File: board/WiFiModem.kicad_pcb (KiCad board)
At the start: 2 copper layers, 88.9 x 57.2 mm, 34 parts, among them J1 DB9_Female, J2 DB25_Male, J3 Barrel_Jack_Switch, J4 PRG, SW1 SW_Push, SW2 SW_Push, U1 ESP-12E, U2 LM7805_TO220, U3 MAX232, U4 LT1117-3.3

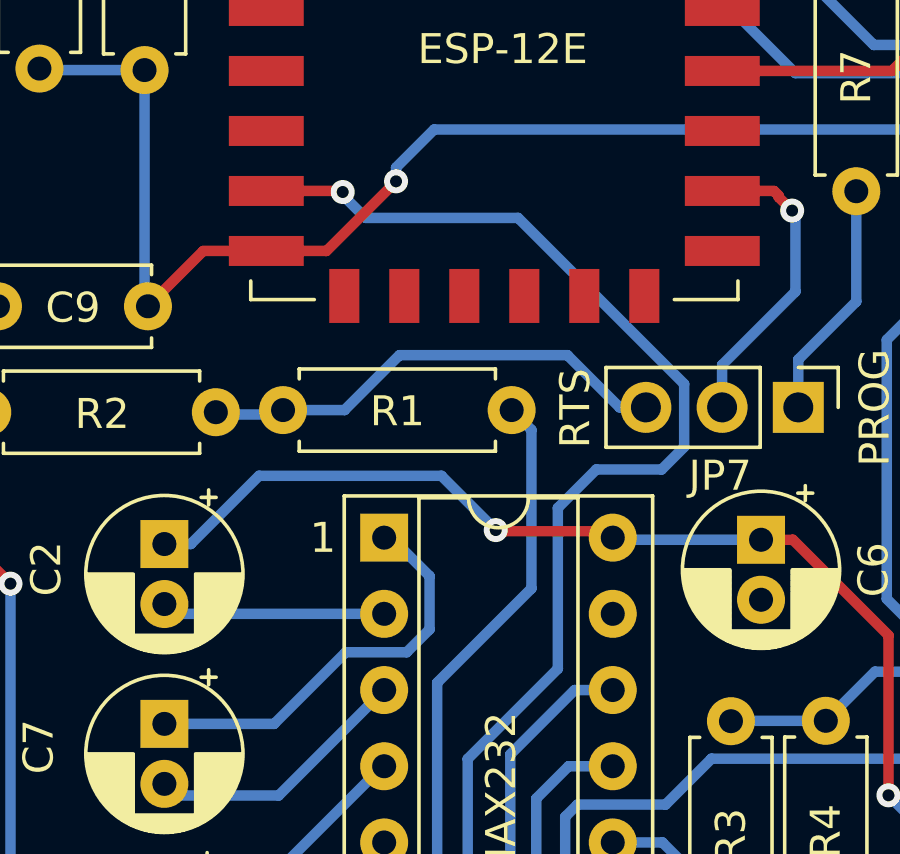
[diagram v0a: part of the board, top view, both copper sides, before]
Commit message: swap RTS and CTS
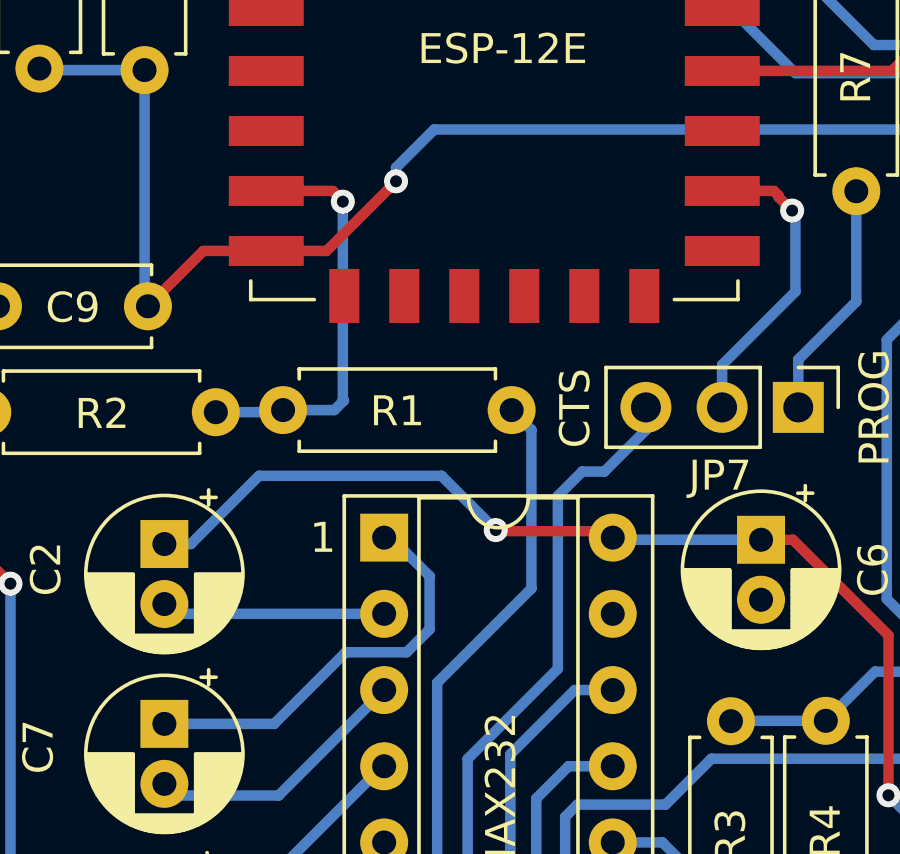
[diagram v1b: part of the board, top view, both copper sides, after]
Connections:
- JP7 pad 3: Net-(R1-Pad2) -> Net-(JP7-Pad3)
- U1 pad 7: Net-(U1-Pad7) -> Net-(R1-Pad2)
- U3 pad 10: Net-(U1-Pad7) -> Net-(JP7-Pad3)
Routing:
- net Net-(U1-Pad7): track 45.8 -> 0.00 mm, vias 2 -> 0
- net Net-(JP7-Pad3): track 0.00 -> 27.0 mm, vias 0 -> 1
- net Net-(R1-Pad2): track 15.9 -> 13.7 mm, vias 0 -> 1

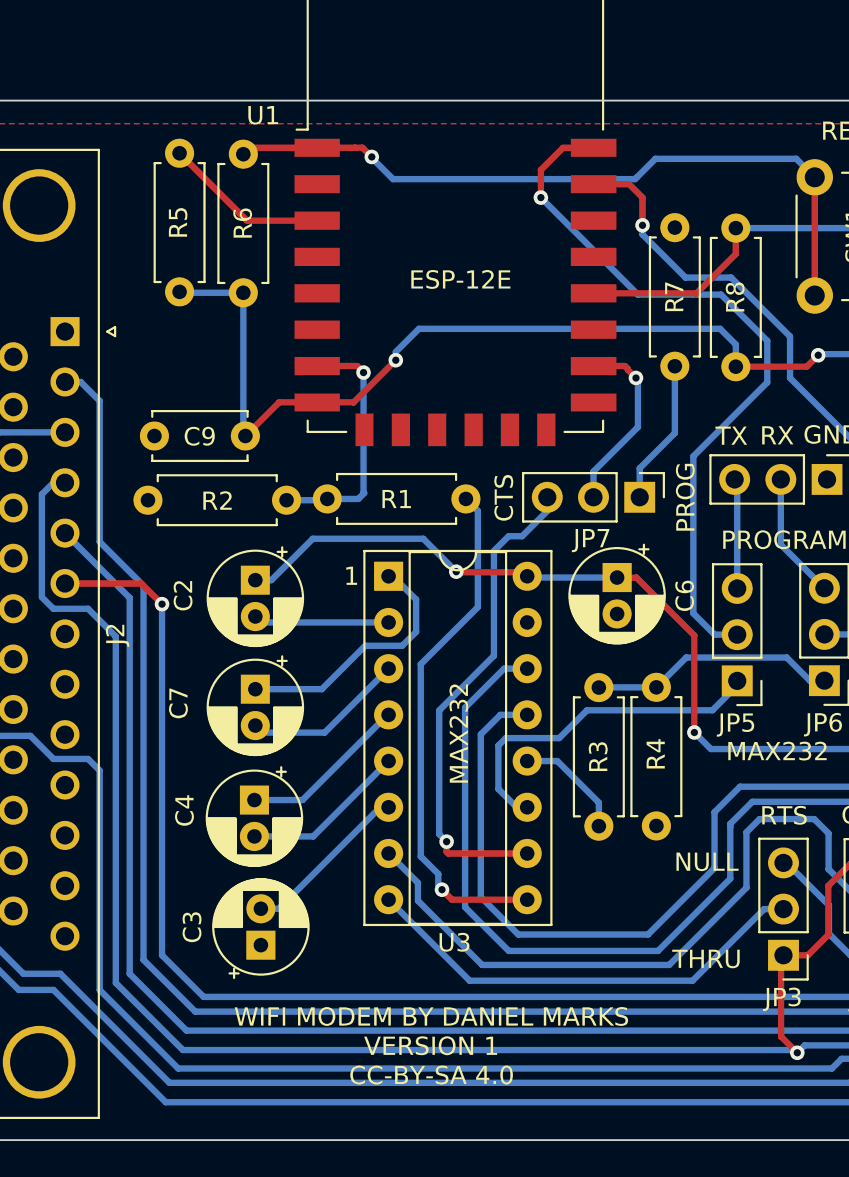
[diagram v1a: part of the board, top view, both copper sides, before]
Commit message: Added flow control enable GPIO
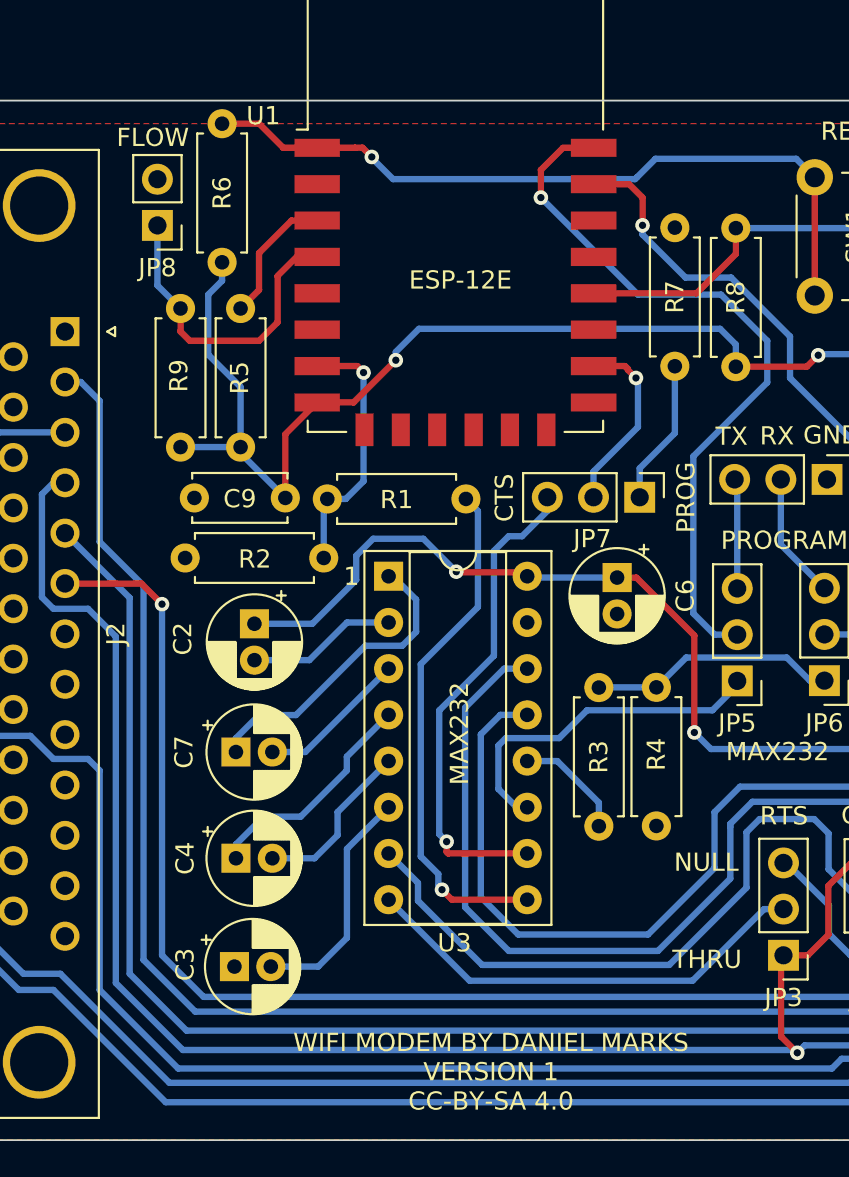
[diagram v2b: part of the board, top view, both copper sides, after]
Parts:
- added JP8: RTSCTS, Connector_PinHeader_2.54mm:PinHeader_1x02_P2.54mm_Vertical, F.Cu at (87.6, 76.7)
- added R9: 10k, Resistor_THT:R_Axial_DIN0207_L6.3mm_D2.5mm_P7.62mm_Horizontal, F.Cu at (88.9, 81.3)
- moved R5 9.17 mm to (92.2, 88.9)
- moved C9 4.05 mm to (89.7, 91.7)
- moved R2 3.78 mm to (96.8, 95.0)
- moved C7 3.62 mm to (91.9, 105.7), turned to 0 degrees
- moved C4 3.36 mm to (91.9, 111.5), turned to 0 degrees
- moved C2 2.40 mm to (93.0, 98.6)
- moved R6 2.04 mm to (91.2, 78.7)
- moved C3 1.87 mm to (91.9, 117.5), turned to 0 degrees
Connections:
- U1 pad 4: unconnected-(U1-Pad4) -> Net-(U1-Pad4)
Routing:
- net Net-(U1-Pad4): track 0.00 -> 17.5 mm
- net +3V3: track 81.1 -> 89.2 mm
- net Net-(C3-Pad2): track 9.33 -> 13.0 mm
- net Net-(C4-Pad1): track 9.32 -> 12.6 mm
- net Net-(C7-Pad1): track 14.0 -> 16.9 mm
- net +5V: track 105.6 -> 107.4 mm
- net Net-(R5-Pad2): track 9.10 -> 7.40 mm
- net Net-(R6-Pad2): track 39.7 -> 41.3 mm
- net Net-(R1-Pad2): track 13.7 -> 14.5 mm
- net Net-(C2-Pad2): track 7.46 -> 8.23 mm
- net Net-(C7-Pad2): track 8.94 -> 8.29 mm
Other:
- board text added: "FLOW"

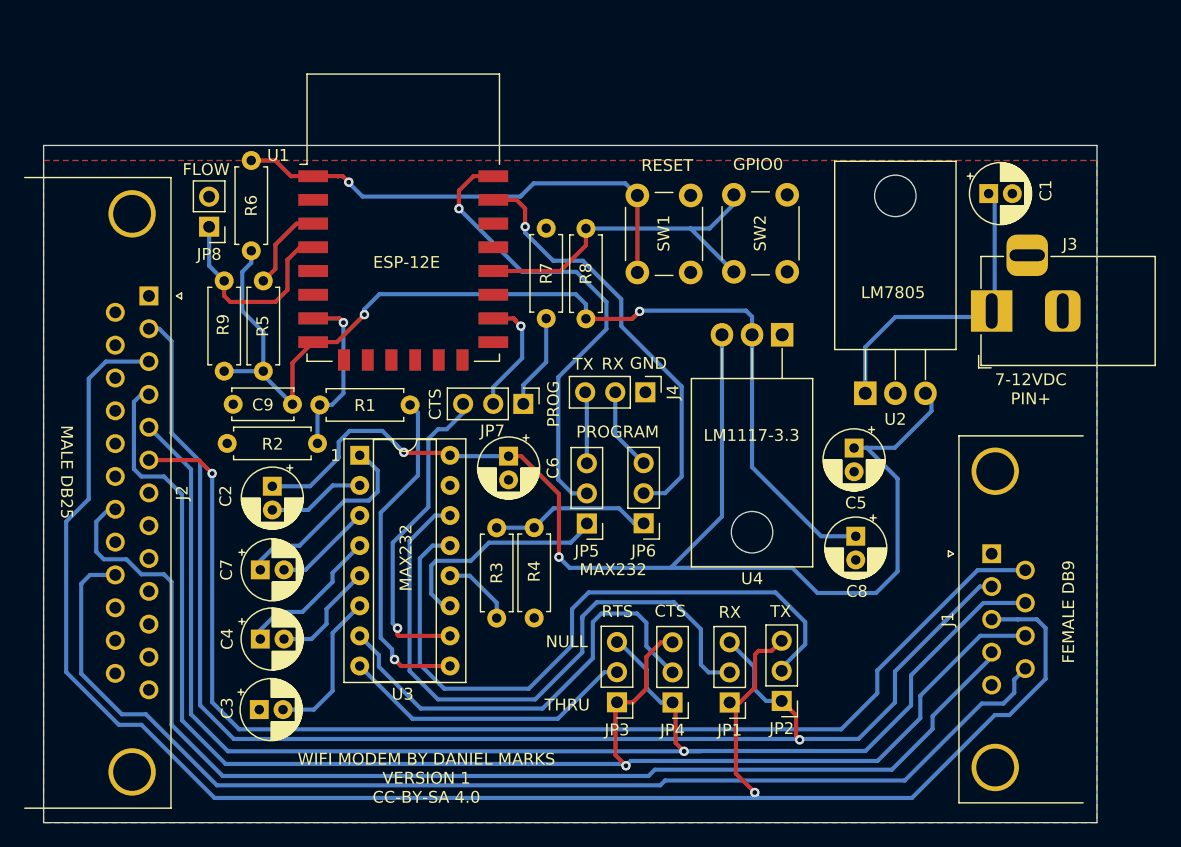
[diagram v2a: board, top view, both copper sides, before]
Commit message: Added all of the other control signals
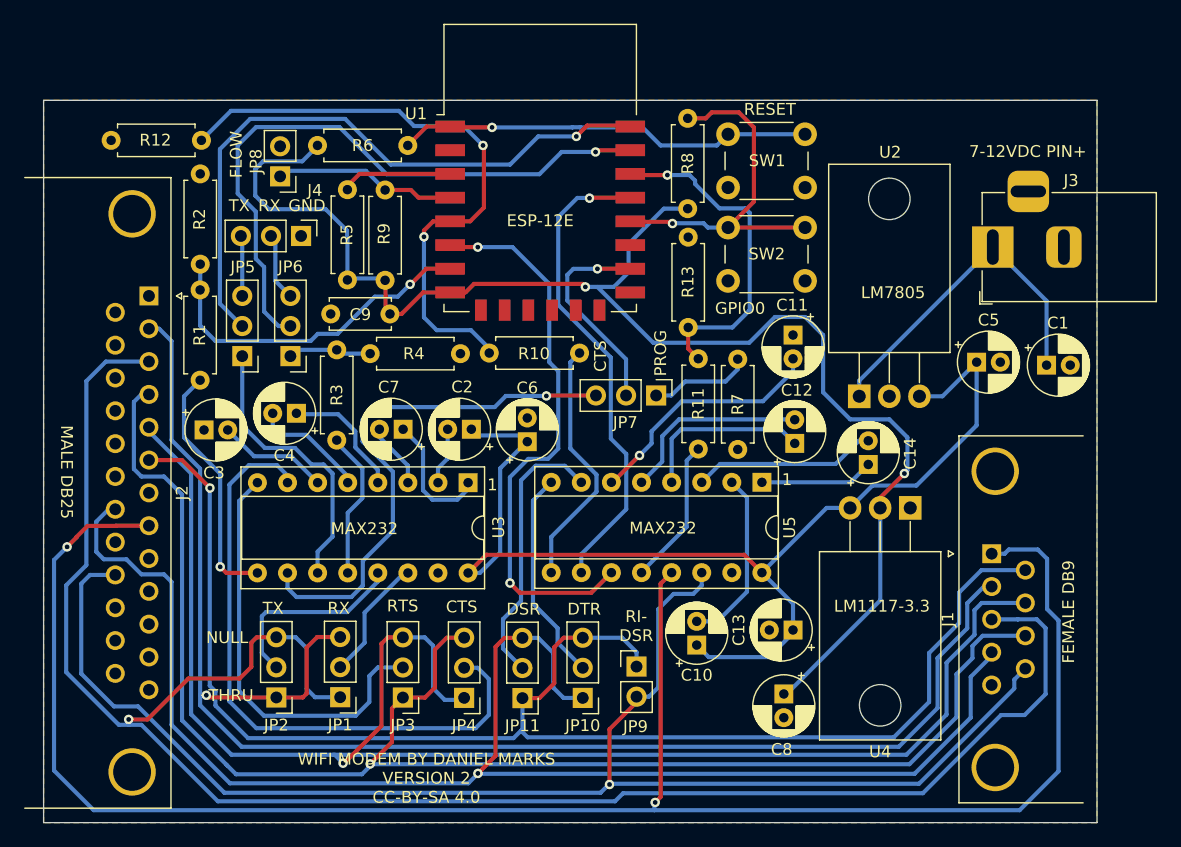
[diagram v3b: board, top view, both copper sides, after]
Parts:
- added C10: 1 uF, Capacitor_THT:CP_Radial_D5.0mm_P2.00mm, F.Cu at (128.8, 112.0)
- added C11: 1 uF, Capacitor_THT:CP_Radial_D5.0mm_P2.00mm, F.Cu at (136.9, 85.9)
- added C12: 1 uF, Capacitor_THT:CP_Radial_D5.0mm_P2.00mm, F.Cu at (137.1, 95.0)
- added C13: 1 uF, Capacitor_THT:CP_Radial_D5.0mm_P2.00mm, F.Cu at (136.9, 110.7)
- added C14: 1 uF, Capacitor_THT:CP_Radial_D5.0mm_P2.00mm, F.Cu at (143.3, 96.8)
- added JP10: DTRB, Connector_PinHeader_2.54mm:PinHeader_1x03_P2.54mm_Vertical, F.Cu at (119.2, 116.5)
- added JP11: DTRB, Connector_PinHeader_2.54mm:PinHeader_1x03_P2.54mm_Vertical, F.Cu at (114.1, 116.5)
- added JP9: RIDSR, Connector_PinHeader_2.54mm:PinHeader_1x02_P2.54mm_Vertical, F.Cu at (123.7, 113.8)
- added R10: 470R, Resistor_THT:R_Axial_DIN0207_L6.3mm_D2.5mm_P7.62mm_Horizontal, F.Cu at (118.9, 87.4)
- added R11: 470R, Resistor_THT:R_Axial_DIN0207_L6.3mm_D2.5mm_P7.62mm_Horizontal, F.Cu at (128.9, 95.5)
- added R12: 1k, Resistor_THT:R_Axial_DIN0207_L6.3mm_D2.5mm_P7.62mm_Horizontal, F.Cu at (87.0, 69.4)
- added R13: 1k, Resistor_THT:R_Axial_DIN0207_L6.3mm_D2.5mm_P7.62mm_Horizontal, F.Cu at (128.1, 85.2)
- added U5: MAX232, Package_DIP:DIP-16_W7.62mm_Socket, F.Cu at (134.3, 98.3)
- moved JP2 42.7 mm to (93.3, 116.4)
- moved JP6 33.0 mm to (94.5, 87.6)
- moved JP1 32.9 mm to (98.7, 116.4)
- moved JP5 32.3 mm to (90.4, 87.6)
- moved J4 31.9 mm to (95.4, 77.5)
- moved C3 24.1 mm to (87.2, 93.9)
- moved R3 20.2 mm to (98.4, 94.7)
- moved R4 20.2 mm to (101.2, 87.4), turned to 0 degrees
- moved C4 19.3 mm to (95.0, 92.5), turned to 180 degrees
- moved U4 18.2 mm to (146.8, 100.4)
- moved R2 18.1 mm to (86.9, 79.9), turned to 90 degrees
- moved JP3 18.1 mm to (104.0, 116.4)
- moved R1 17.8 mm to (86.9, 89.7), turned to 90 degrees
- moved JP4 17.6 mm to (109.2, 116.5)
- moved C2 17.5 mm to (109.8, 93.8), turned to 180 degrees
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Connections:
- net Net-(JP5-Pad1) renamed GPIO1
- net Net-(JP6-Pad1) renamed GPIO3
- net Net-(JP7-Pad3) renamed GPIO15
- net Net-(R1-Pad2) renamed GPIO13
- J2 pad 8: unconnected-(J2-Pad8) -> DCD
- U1 pad 19: unconnected-(U1-Pad19) -> GPIO4
- U1 pad 20: unconnected-(U1-Pad20) -> GPIO5
- U1 pad 5: unconnected-(U1-Pad5) -> GPIO14
- U1 pad 6: unconnected-(U1-Pad6) -> GPIO12
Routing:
- net DCD: track 0.00 -> 158.7 mm, vias 0 -> 2
- net GPIO14: track 0.00 -> 51.5 mm, vias 0 -> 2
- net GPIO12: track 0.00 -> 47.6 mm, vias 0 -> 2
- net RXDB: track 52.7 -> 10.5 mm
- net GPIO4: track 0.00 -> 40.7 mm, vias 0 -> 1
- net TXDB: track 56.5 -> 16.5 mm
- net +3V3: track 89.2 -> 120.4 mm
- net GPIO5: track 0.00 -> 28.6 mm, vias 0 -> 1
- net DTR: track 100.3 -> 124.9 mm, vias 0 -> 1
- net DSRB: track 0.00 -> 23.3 mm
- net RI: track 99.1 -> 122.1 mm, vias 0 -> 1
- net Net-(R10-Pad1): track 0.00 -> 21.4 mm
- net DSR: track 101.4 -> 122.5 mm
- net Net-(C11-Pad2): track 0.00 -> 20.9 mm, vias 0 -> 1
- net DTRB: track 0.00 -> 18.0 mm
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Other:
- board size 88.9 x 57.2 mm -> 88.9 x 61 mm
- board text added: "DSR"
- board text added: "DTR"
- board text added: "RI- DSR"
- board text added: "WIFI MODEM BY DANIEL MARKS VERSION 2 CC-BY-SA 4.0"
- board text removed: "PROGRAM"
- board text removed: "WIFI MODEM BY DANIEL MARKS VERSION 1 CC-BY-SA 4.0"

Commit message: Changed from DB25 male to DB25 female
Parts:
- J2: value DB25_Male -> DB25_Female; footprint Connector_Dsub:DSUB-25_Male_Horizontal_P2.77x2.84mm_EdgePinOffset7.70mm_Housed_MountingHolesOffset9.12mm -> Connector_Dsub:DSUB-25_Female_Horizontal_P2.77x2.84mm_EdgePinOffset7.70mm_Housed_MountingHolesOffset9.12mm
- moved J2 33.2 mm to (82.5, 115.8)
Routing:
- net RXD: track 159.1 -> 123.3 mm
- net TXD: track 127.9 -> 100.8 mm
- net RI: track 122.1 -> 137.1 mm, vias 1 -> 2
- net RTS: track 127.8 -> 117.5 mm, vias 1 -> 2
- net CTS: track 130.6 -> 122.9 mm
- net DCD: track 158.7 -> 164.4 mm, vias 2 -> 1
- net DSR: track 122.5 -> 117.3 mm, vias 1 -> 0
- net DTR: track 124.9 -> 128.9 mm
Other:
- board text added: "FEMALE DB25"
- board text removed: "MALE DB25"

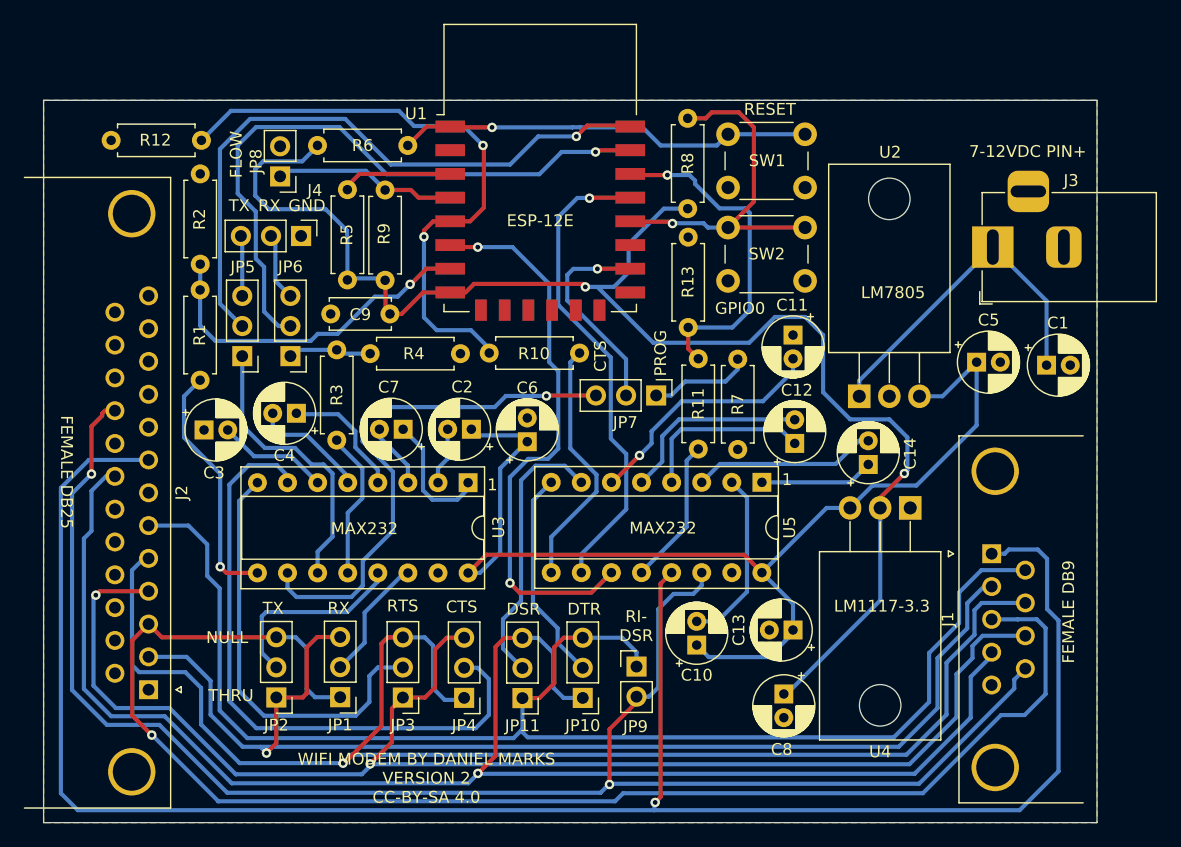
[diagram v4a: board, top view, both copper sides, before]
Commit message: Added silkscreening to indicate male/female sides
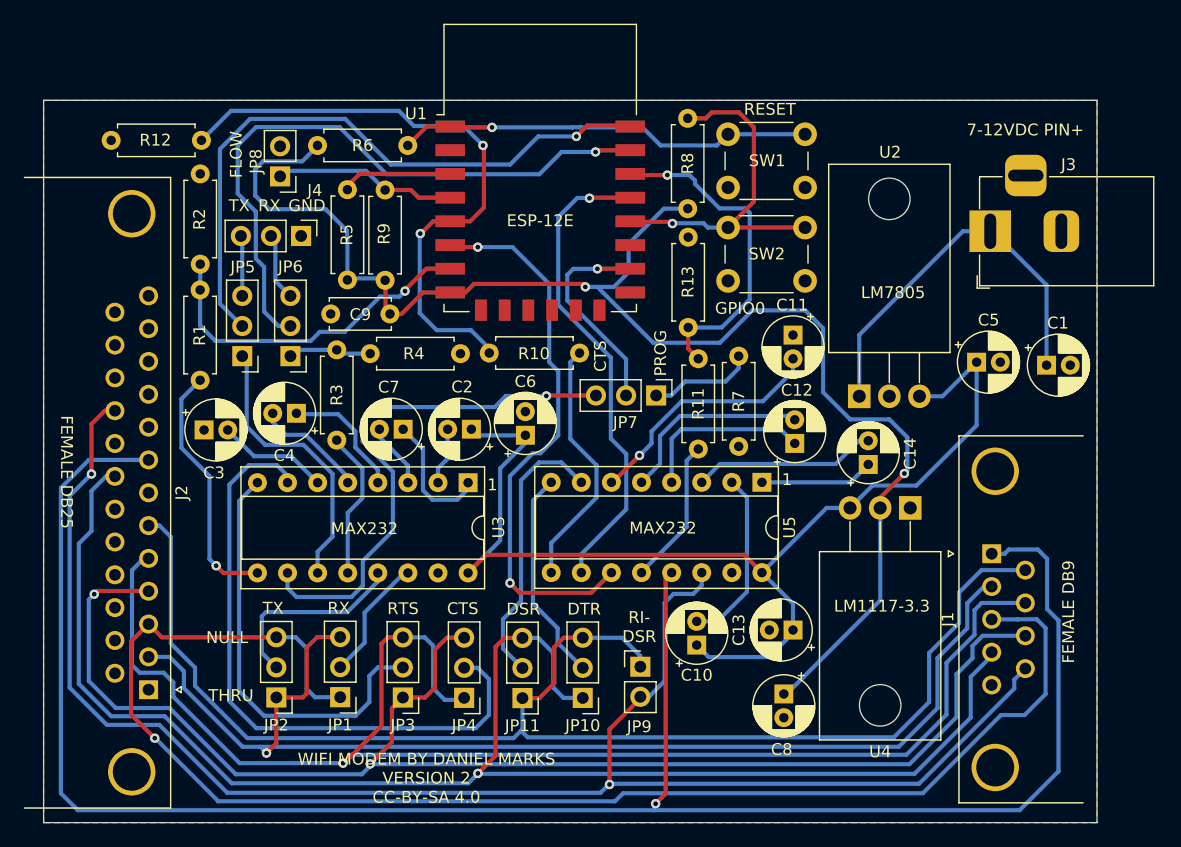
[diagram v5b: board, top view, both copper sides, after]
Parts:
- moved J3 1.35 mm to (153.6, 77.1)
- moved C6 0.56 mm to (114.3, 94.3)
- moved JP9 0.32 mm to (124.0, 113.8)
- moved R7 0.27 mm to (132.3, 87.6)
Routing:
- net Net-(C1-Pad1): track 29.1 -> 33.3 mm
- net DSR: track 117.3 -> 116.0 mm
- net CTS: track 122.9 -> 121.8 mm
- net TXD: track 100.8 -> 100.0 mm
- net +3V3: track 120.4 -> 121.2 mm
- net GPIO12: track 47.6 -> 47.0 mm
- net GPIO5: track 28.6 -> 28.1 mm
- net +5V: track 95.2 -> 94.7 mm
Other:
- board text added: "MALE DB25"
- board text added: "MALE DB9"
